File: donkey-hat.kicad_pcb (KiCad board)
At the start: 2 copper layers, 65 x 56.5 mm, 59 parts, among them J1 6-18V, J14 NEOPIXEL, J15 MPU-9250, J16 4, J17 5, J18 6, J19 7, J2 Raspberry_Pi_2_3, J24 3mm_Mount, J25 3mm_Mount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

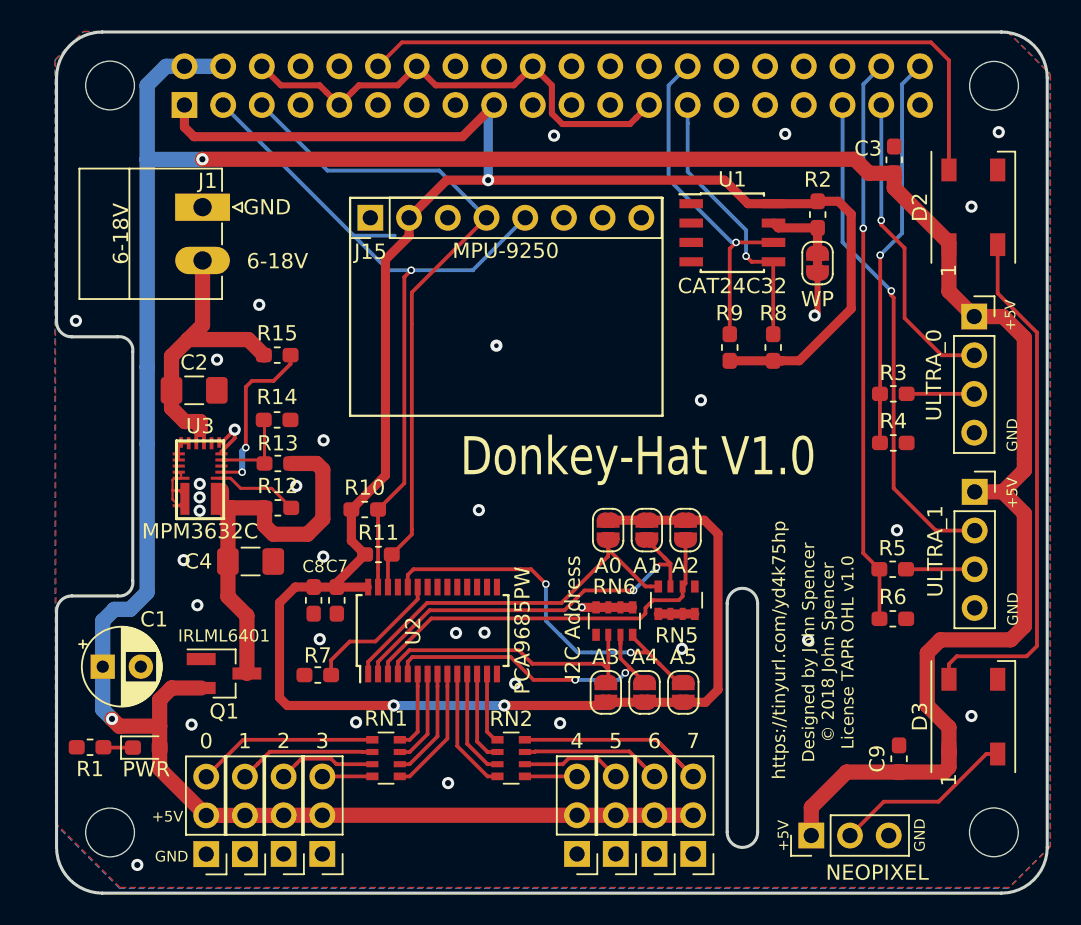
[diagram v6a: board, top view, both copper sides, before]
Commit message: Added Regulator Bypass.
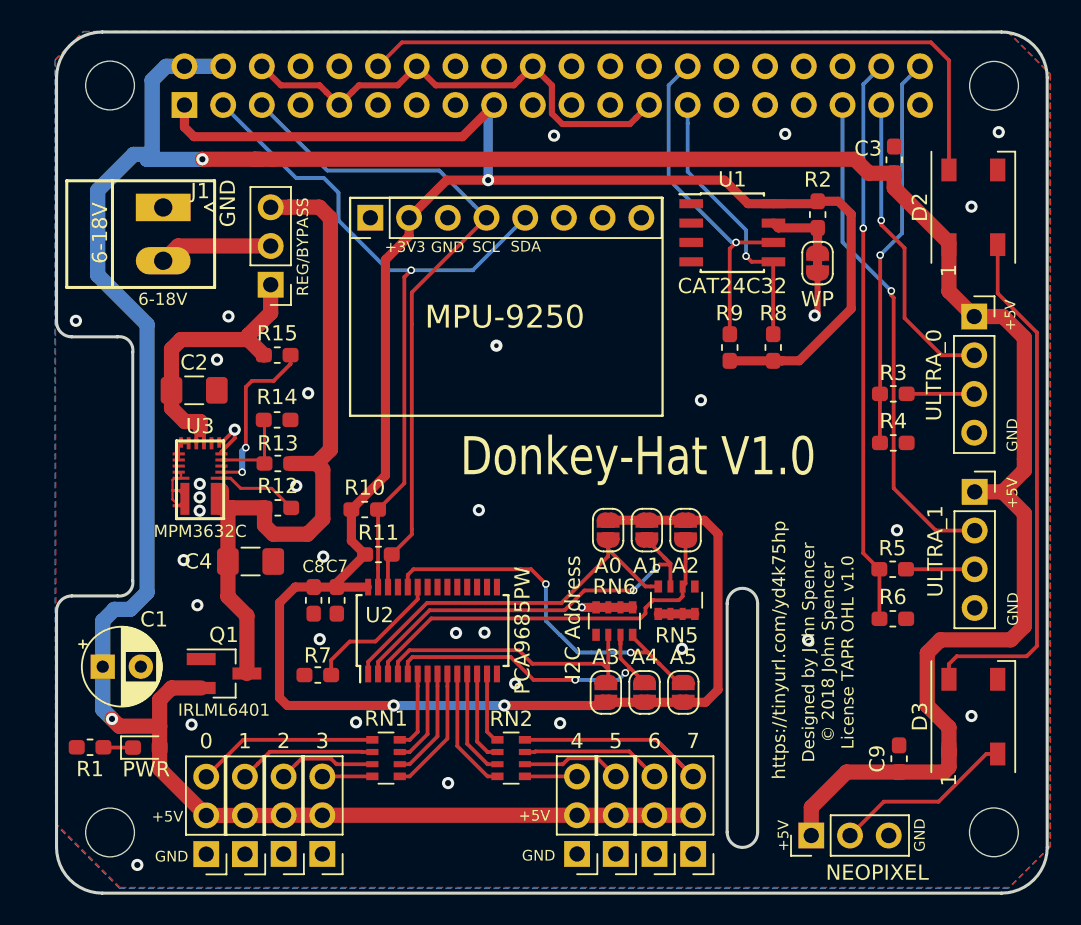
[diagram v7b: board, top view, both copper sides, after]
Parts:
- added J5: REG/BYPASS, Connector_PinHeader_2.54mm:PinHeader_1x03_P2.54mm_Vertical, F.Cu at (92.6, 77.4)
- J1: footprint Connector_Phoenix_MC:PhoenixContact_MC_1,5_2-G-3.5_1x02_P3.50mm_Horizontal -> libs:ScrewTerminal-Small
- moved J1 3.13 mm to (85.5, 74.1)
- moved G*** 2.07 mm to (90.4, 89.9)
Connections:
- net Net-(C4-Pad1) renamed /REG
- C2 pad 1: Net-(C2-Pad1) -> /VIN_REG
- J1 pad 2: Net-(C2-Pad1) -> /VIN
- R15 pad 1: Net-(C2-Pad1) -> /VIN_REG
- U3 pad 17: Net-(C2-Pad1) -> /VIN_REG
- U3 pad 18: Net-(C2-Pad1) -> /VIN_REG
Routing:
- net Net-(C2-Pad1): track 21.8 -> 0.00 mm
- net /REG: track 26.5 -> 47.2 mm
- net /VIN_REG: track 0.00 -> 20.7 mm
- net /VIN: track 0.00 -> 7.45 mm
- net +5V: track 210.4 -> 214.6 mm
- net /SDA_3.3: track 55.7 -> 54.0 mm
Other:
- board text added: "+3V3"
- board text added: "SCL"
- board text added: "SDA"

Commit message: Added logos and call outs.
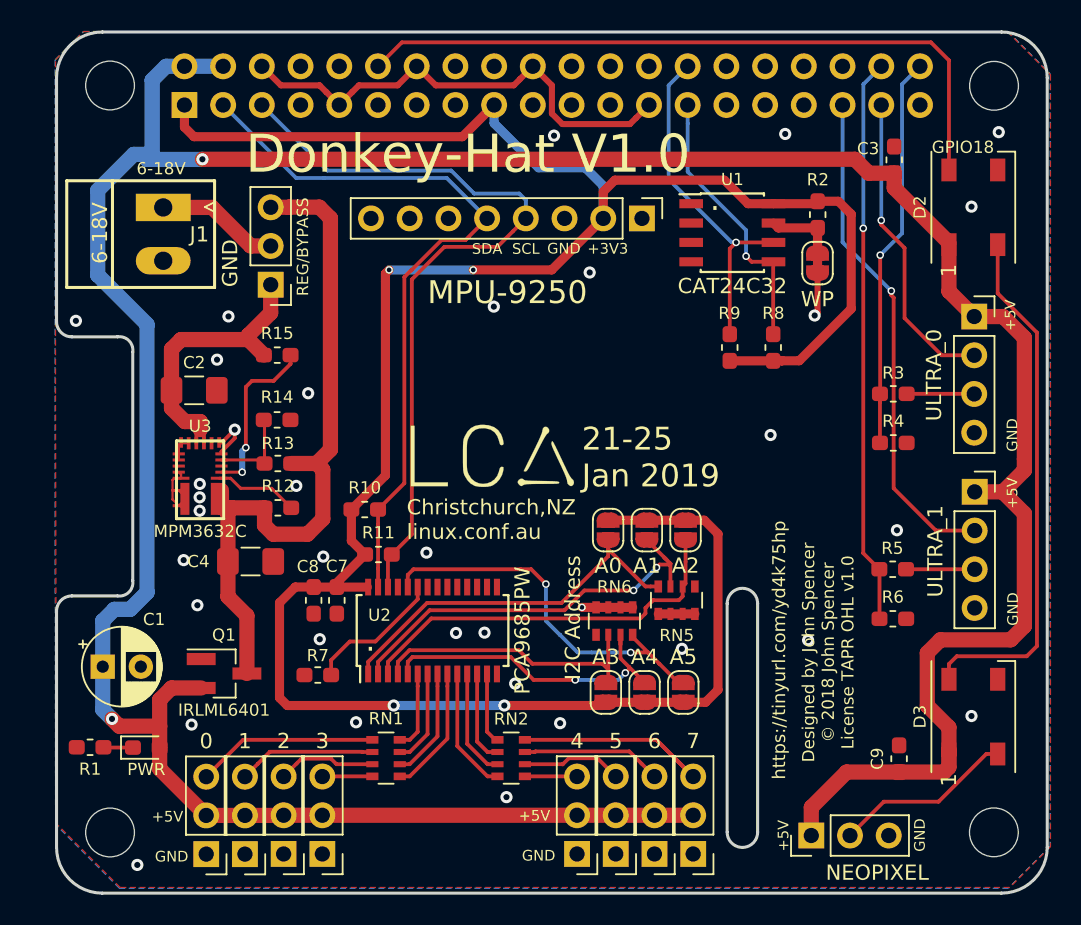
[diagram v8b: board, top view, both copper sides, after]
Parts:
- removed the G*** at (90.4, 89.9)
- added G***: LOGO, libs:logo.cchs, B.Cu at (92.3, 100.5)
- added G***: LOGO, libs:logo.thingc, B.Cu at (111.8, 103.9)
- added G***: LOGO, libs:logo.LCA, F.Cu at (107.1, 88.6)
- added G***: LOGO, libs:logo.HeartOfPluto2, B.Cu at (132.2, 102.2)
- added G***: LOGO, libs:logo.linuxau.silk, B.Cu at (114.4, 87.2)
- added G***: LOGO, libs:logo.linuxau.mask, B.Cu at (114.4, 87.0)
- moved J15 17.8 mm to (116.9, 73.0), turned to 270 degrees
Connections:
- J1 pad 1: GND -> /VIN
- J1 pad 2: /VIN -> GND
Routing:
- net +3V3: track 162.3 -> 169.7 mm, vias 3 -> 4
- net /SCL_3.3: track 45.1 -> 51.4 mm
- net /SDA_3.3: track 54.0 -> 48.5 mm, vias 1 -> 0
- net /VIN: track 7.45 -> 8.10 mm
- net GND: vias 34 -> 35
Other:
- board text added: "."
- board text added: "21-25 Jan 2019"
- board text added: "Australia"
- board text added: "Christchurch,NZ linux.conf.au"
- board text added: "Follow us: @mage0r @geekscape @jonoxer @thingc @heartofpluto_ @linuxaustralia @hackmelbourne"
- board text added: "GPIO18"
- board text added: "LINUX"
- board text added: "Proudly Sponsored by"
- board text added: "hackmelbourne.org"
- board text added: "heartofpluto.co"
- board text added: "linux.org.au"
- board text added: "thingc.co"
